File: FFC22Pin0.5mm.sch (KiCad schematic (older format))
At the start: 4 parts

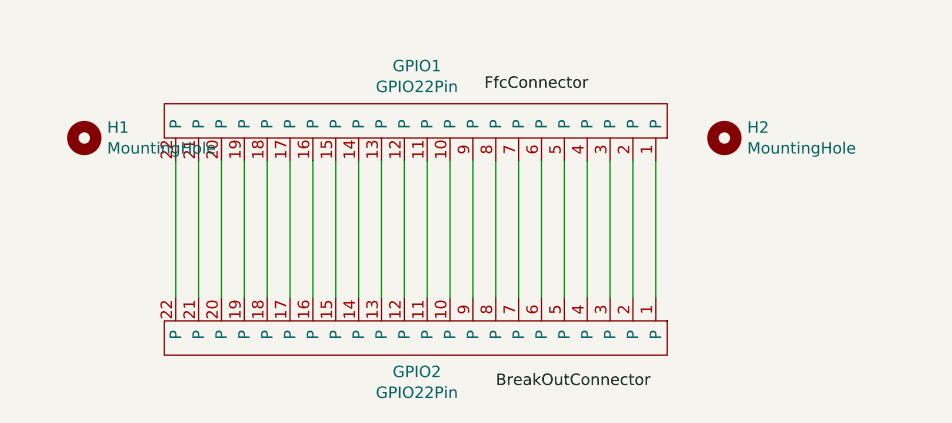
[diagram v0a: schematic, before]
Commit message: 基板裏にベタ追加、ビア追加、パッドをベタに接続、配線をより対称に近づけた
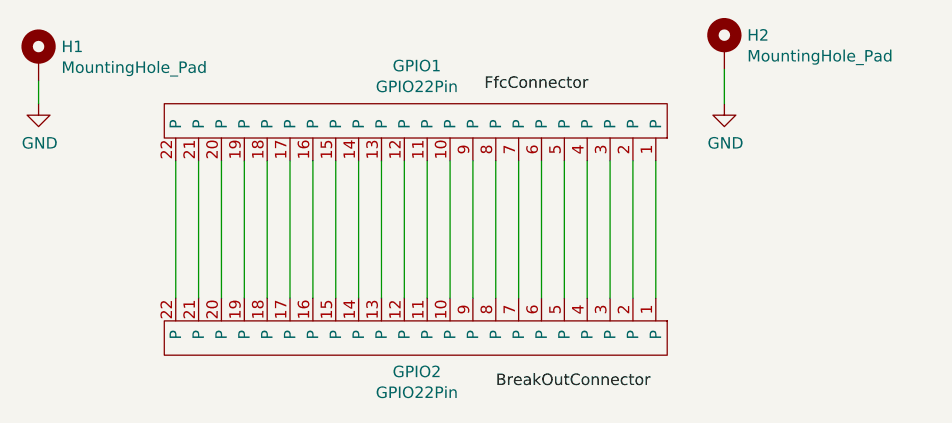
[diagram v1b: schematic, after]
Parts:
- removed H1, H2: MountingHole, MountingHole:MountingHole_3.2mm_M3_Pad_TopBottom, symbol Mechanical:MountingHole
- added H1, H2: MountingHole_Pad, symbol Mechanical:MountingHole_Pad
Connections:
- new net GND: H1.1, H2.1
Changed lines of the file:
@@
 	4350 2300 4350 2900
 $Comp
-L Mechanical:MountingHole H1
-U 1 1 5FFC62F7
-P 1850 2200
-F 0 "H1" H 1950 2246 50  0000 L CNN
-F 1 "MountingHole" H 1950 2155 50  0000 L CNN
-F 2 "MountingHole:MountingHole_3.2mm_M3_Pad_TopBottom" H 1850 2200 50  0001 C CNN
-F 3 "~" H 1850 2200 50  0001 C CNN
-	1    1850 2200
+L Mechanical:MountingHole_Pad H1
+U 1 1 5FFEEFC1
+P 1650 1850
+F 0 "H1" H 1750 1899 50  0000 L CNN
+F 1 "MountingHole_Pad" H 1750 1808 50  0000 L CNN
+F 2 "" H 1650 1850 50  0001 C CNN
+F 3 "~" H 1650 1850 50  0001 C CNN
+	1    1650 1850
 	1    0    0    -1
 $EndComp
 $Comp
-L Mechanical:MountingHole H2
-U 1 1 5FFC6A23
-P 4650 2200
-F 0 "H2" H 4750 2246 50  0000 L CNN
-F 1 "MountingHole" H 4750 2155 50  0000 L CNN
-F 2 "MountingHole:MountingHole_3.2mm_M3_Pad_TopBottom" H 4650 2200 50  0001 C CNN
-F 3 "~" H 4650 2200 50  0001 C CNN
-	1    4650 2200
+L power:GND #PWR0101
+U 1 1 5FFEFDB2
+P 1650 2050
+F 0 "#PWR0101" H 1650 1800 50  0001 C CNN
+F 1 "GND" H 1655 1877 50  0000 C CNN
+F 2 "" H 1650 2050 50  0001 C CNN
+F 3 "" H 1650 2050 50  0001 C CNN
+	1    1650 2050
 	1    0    0    -1
 $EndComp
+Wire Wire Line
+	1650 1950 1650 2050
+Wire Wire Line
+	4650 1900 4650 2050
+$Comp
+L power:GND #PWR0102
+U 1 1 5FFF0D62
+P 4650 2050
+F 0 "#PWR0102" H 4650 1800 50  0001 C CNN
+F 1 "GND" H 4655 1877 50  0000 C CNN
+F 2 "" H 4650 2050 50  0001 C CNN
+F 3 "" H 4650 2050 50  0001 C CNN
+	1    4650 2050
+	1    0    0    -1
+$EndComp
+$Comp
+L Mechanical:MountingHole_Pad H2
+U 1 1 5FFF0D5C
+P 4650 1800
+F 0 "H2" H 4750 1849 50  0000 L CNN
+F 1 "MountingHole_Pad" H 4750 1758 50  0000 L CNN
+F 2 "" H 4650 1800 50  0001 C CNN
+F 3 "~" H 4650 1800 50  0001 C CNN
+	1    4650 1800
+	1    0    0    -1
+$EndComp
